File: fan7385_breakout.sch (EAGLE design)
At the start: 13 parts

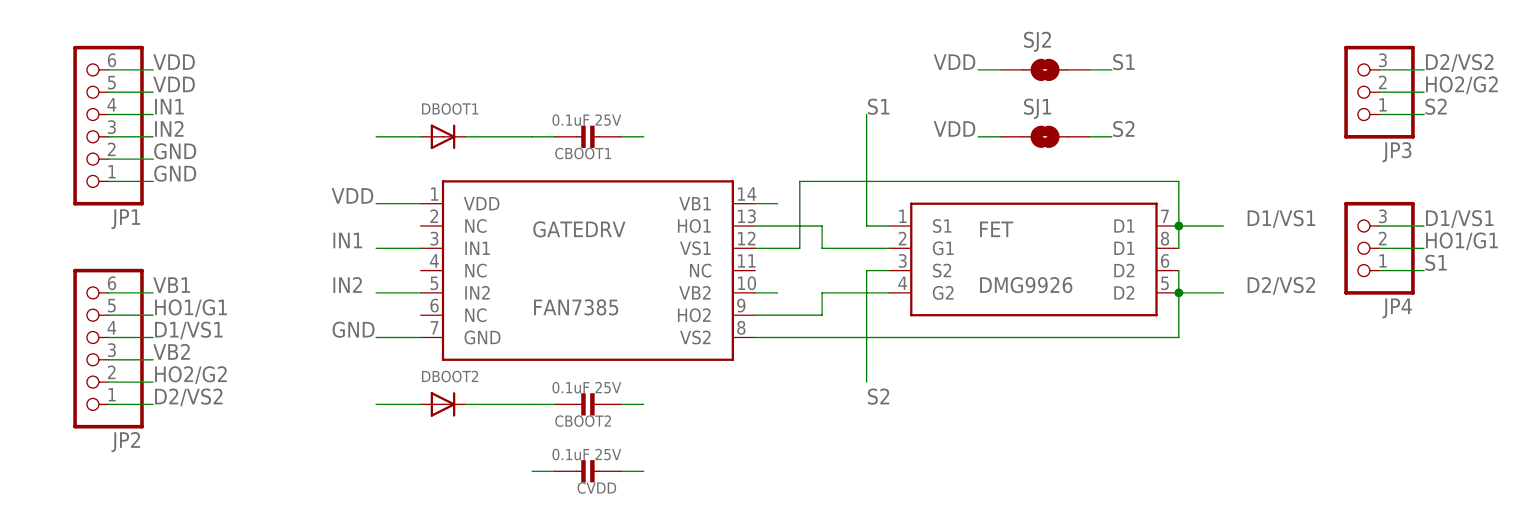
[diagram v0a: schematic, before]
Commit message: make the signal back from drains to the driver normal instead of high-power
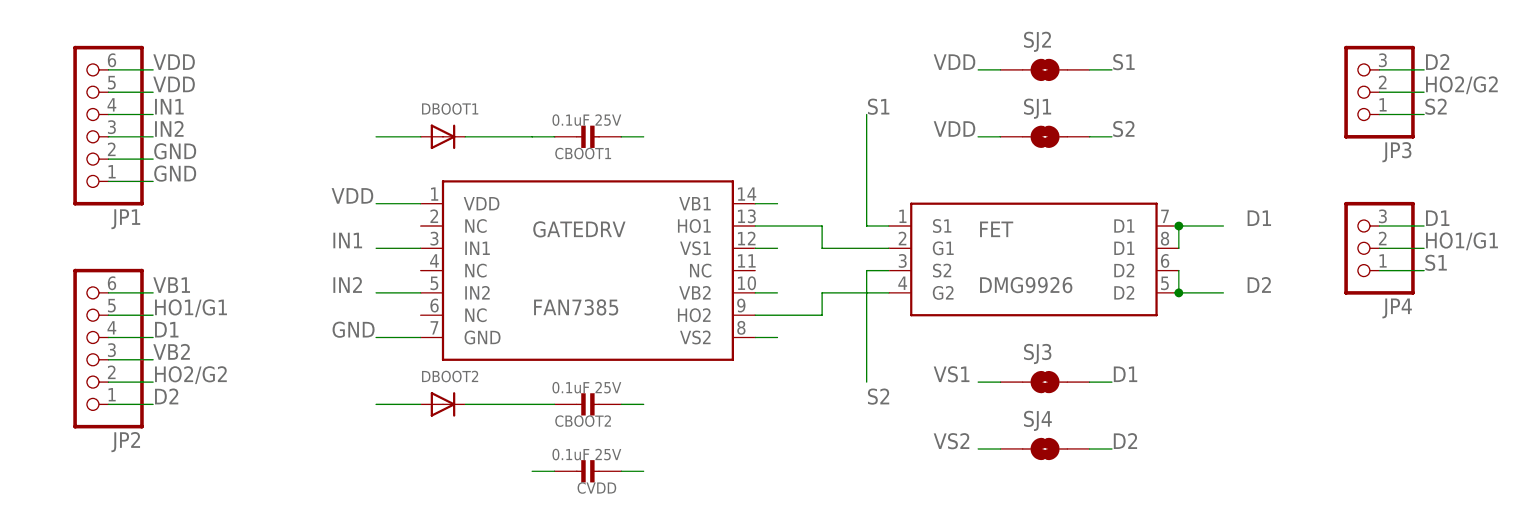
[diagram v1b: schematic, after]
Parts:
- added SJ3, SJ4: SOLDERJUMPERTRACE, SparkFun-Passives:SOLDERJUMPERTRACE
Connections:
- removed net D1/VS1: CBOOT1.P$1, FET.D1@1, FET.D1@2, GATEDRV.VS1, JP2.4, JP4.3
- removed net D2/VS2: CBOOT2.P$1, FET.D2@1, FET.D2@2, GATEDRV.VS2, JP2.1, JP3.3
- new net D1: CBOOT1.P$1, FET.D1@1, FET.D1@2, JP2.4, JP4.3, SJ3.2
- new net D2: CBOOT2.P$1, FET.D2@1, FET.D2@2, JP2.1, JP3.3, SJ4.2
- new net VS1: GATEDRV.VS1, SJ3.1
- new net VS2: GATEDRV.VS2, SJ4.1
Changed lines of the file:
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@@
 <part name="JP3" library="pinhead" deviceset="PINHD-1X3" device=""/>
 <part name="JP4" library="pinhead" deviceset="PINHD-1X3" device=""/>
+<part name="SJ3" library="SparkFun-Passives" deviceset="SOLDERJUMPER" device="TRACE"/>
+<part name="SJ4" library="SparkFun-Passives" deviceset="SOLDERJUMPER" device="TRACE"/>
 </parts>
 <sheets>
@@
 <instance part="JP3" gate="A" x="142.24" y="55.88" rot="R180"/>
 <instance part="JP4" gate="A" x="142.24" y="38.1" rot="R180"/>
+<instance part="SJ3" gate="1" x="106.68" y="22.86" smashed="yes">
+<attribute name="NAME" x="104.14" y="25.4" size="1.778" layer="95"/>
+</instance>
+<instance part="SJ4" gate="1" x="106.68" y="15.24" smashed="yes">
+<attribute name="NAME" x="104.14" y="17.78" size="1.778" layer="95"/>
+</instance>
 </instances>
 <busses>
@@
 </segment>
 </net>
-<net name="D2/VS2" class="2">
+<net name="D2" class="2">
 <segment>
 <pinref part="FET" gate="G$1" pin="D2@1"/>
@@
 <junction x="121.92" y="33.02"/>
 <label x="129.54" y="33.02" size="1.778" layer="95"/>
-<pinref part="GATEDRV" gate="G$1" pin="VS2"/>
-<wire x1="73.66" y1="27.94" x2="121.92" y2="27.94" width="0.1524" layer="91"/>
-<wire x1="121.92" y1="27.94" x2="121.92" y2="33.02" width="0.1524" layer="91"/>
 </segment>
 <segment>
@@
 <label x="149.86" y="58.42" size="1.778" layer="95"/>
 </segment>
-</net>
-<net name="D1/VS1" class="2">
+<segment>
+<pinref part="SJ4" gate="1" pin="2"/>
+<wire x1="111.76" y1="15.24" x2="114.3" y2="15.24" width="0.1524" layer="91"/>
+<label x="114.3" y="15.24" size="1.778" layer="95"/>
+</segment>
+</net>
+<net name="D1" class="2">
 <segment>
 <pinref part="FET" gate="G$1" pin="D1@1"/>
@@
 <junction x="121.92" y="40.64"/>
 <label x="129.54" y="40.64" size="1.778" layer="95"/>
-<wire x1="121.92" y1="40.64" x2="121.92" y2="45.72" width="0.1524" layer="91"/>
-<wire x1="121.92" y1="45.72" x2="78.74" y2="45.72" width="0.1524" layer="91"/>
-<wire x1="78.74" y1="45.72" x2="78.74" y2="38.1" width="0.1524" layer="91"/>
-<pinref part="GATEDRV" gate="G$1" pin="VS1"/>
-<wire x1="78.74" y1="38.1" x2="73.66" y2="38.1" width="0.1524" layer="91"/>
 </segment>
 <segment>
@@
 <label x="149.86" y="40.64" size="1.778" layer="95"/>
 </segment>
-</net>
+<segment>
+<pinref part="SJ3" gate="1" pin="2"/>
+<wire x1="111.76" y1="22.86" x2="114.3" y2="22.86" width="0.1524" layer="91"/>
+<label x="114.3" y="22.86" size="1.778" layer="95"/>
+</segment>
+</net>
+<net name="VS1" class="0">
+<segment>
+<pinref part="GATEDRV" gate="G$1" pin="VS1"/>
+<wire x1="76.2" y1="38.1" x2="73.66" y2="38.1" width="0.1524" layer="91"/>
+</segment>
+<segment>
+<pinref part="SJ3" gate="1" pin="1"/>
+<wire x1="101.6" y1="22.86" x2="99.06" y2="22.86" width="0.1524" layer="91"/>
+<label x="93.98" y="22.86" size="1.778" layer="95"/>
+</segment>
+</net>
+<net name="VS2" class="0">
+<segment>
+<pinref part="GATEDRV" gate="G$1" pin="VS2"/>
+<wire x1="73.66" y1="27.94" x2="76.2" y2="27.94" width="0.1524" layer="91"/>
+</segment>
+<segment>
+<pinref part="SJ4" gate="1" pin="1"/>
+<wire x1="101.6" y1="15.24" x2="99.06" y2="15.24" width="0.1524" layer="91"/>
+<label x="93.98" y="15.24" size="1.778" layer="95"/>
+</segment>
+</net>

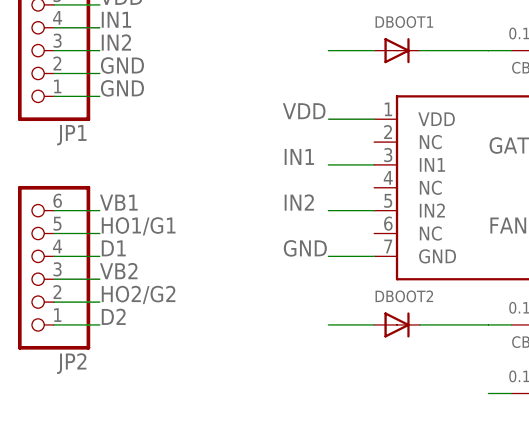
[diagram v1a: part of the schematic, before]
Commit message: one more signal rename
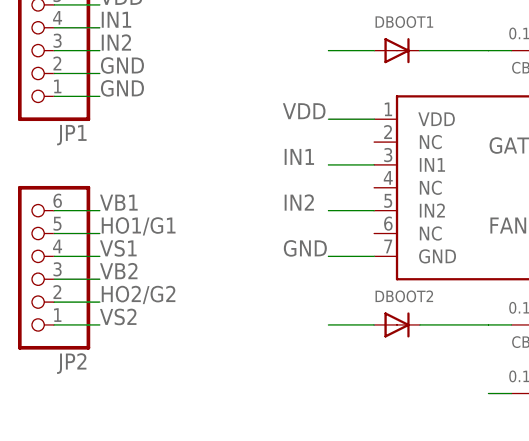
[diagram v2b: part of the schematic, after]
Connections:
- net D1: no longer JP2.4
- net D2: no longer JP2.1
- net VS1: now also JP2.4
- net VS2: now also JP2.1
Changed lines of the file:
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@@
-</segment>
-<segment>
-<pinref part="JP2" gate="A" pin="1"/>
-<wire x1="0" y1="20.32" x2="5.08" y2="20.32" width="0.1524" layer="91"/>
-<label x="5.08" y="20.32" size="1.778" layer="95"/>
 </segment>
 <segment>
@@
 </segment>
 <segment>
-<pinref part="JP2" gate="A" pin="4"/>
-<wire x1="0" y1="27.94" x2="5.08" y2="27.94" width="0.1524" layer="91"/>
-<label x="5.08" y="27.94" size="1.778" layer="95"/>
-</segment>
-<segment>
 <pinref part="JP4" gate="A" pin="3"/>
 <wire x1="144.78" y1="40.64" x2="149.86" y2="40.64" width="0.1524" layer="91"/>
@@
 <label x="93.98" y="22.86" size="1.778" layer="95"/>
 </segment>
+<segment>
+<pinref part="JP2" gate="A" pin="4"/>
+<wire x1="0" y1="27.94" x2="5.08" y2="27.94" width="0.1524" layer="91"/>
+<label x="5.08" y="27.94" size="1.778" layer="95"/>
+</segment>
 </net>
 <net name="VS2" class="0">
@@
 <label x="93.98" y="15.24" size="1.778" layer="95"/>
 </segment>
+<segment>
+<pinref part="JP2" gate="A" pin="1"/>
+<wire x1="0" y1="20.32" x2="5.08" y2="20.32" width="0.1524" layer="91"/>
+<label x="5.08" y="20.32" size="1.778" layer="95"/>
+</segment>
 </net>

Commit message: one more signal rename
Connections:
- net D1: no longer CBOOT1.P$1
- net D2: no longer CBOOT2.P$1
- net VS1: now also CBOOT1.P$1
- net VS2: now also CBOOT2.P$1
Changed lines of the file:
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@@
-</segment>
-<segment>
-<pinref part="CBOOT2" gate="G$1" pin="P$1"/>
-<wire x1="58.42" y1="20.32" x2="60.96" y2="20.32" width="0.1524" layer="91"/>
 </segment>
 <segment>
@@
 <junction x="121.92" y="40.64"/>
 <label x="129.54" y="40.64" size="1.778" layer="95"/>
-</segment>
-<segment>
-<pinref part="CBOOT1" gate="G$1" pin="P$1"/>
-<wire x1="58.42" y1="50.8" x2="60.96" y2="50.8" width="0.1524" layer="91"/>
 </segment>
 <segment>
@@
 <label x="5.08" y="27.94" size="1.778" layer="95"/>
 </segment>
+<segment>
+<pinref part="CBOOT1" gate="G$1" pin="P$1"/>
+<wire x1="58.42" y1="50.8" x2="60.96" y2="50.8" width="0.1524" layer="91"/>
+</segment>
 </net>
 <net name="VS2" class="0">
@@
 <label x="5.08" y="20.32" size="1.778" layer="95"/>
 </segment>
+<segment>
+<pinref part="CBOOT2" gate="G$1" pin="P$1"/>
+<wire x1="58.42" y1="20.32" x2="60.96" y2="20.32" width="0.1524" layer="91"/>
+</segment>
 </net>

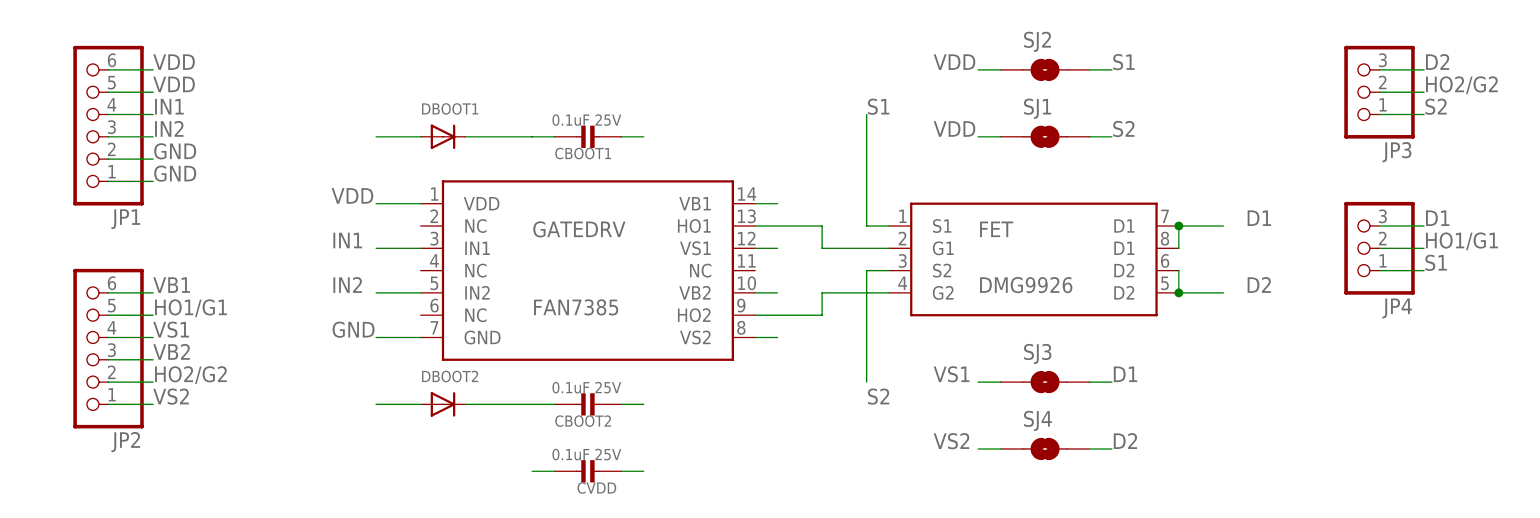
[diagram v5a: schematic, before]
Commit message: diffeent pin header part and 100mil spacing between pins
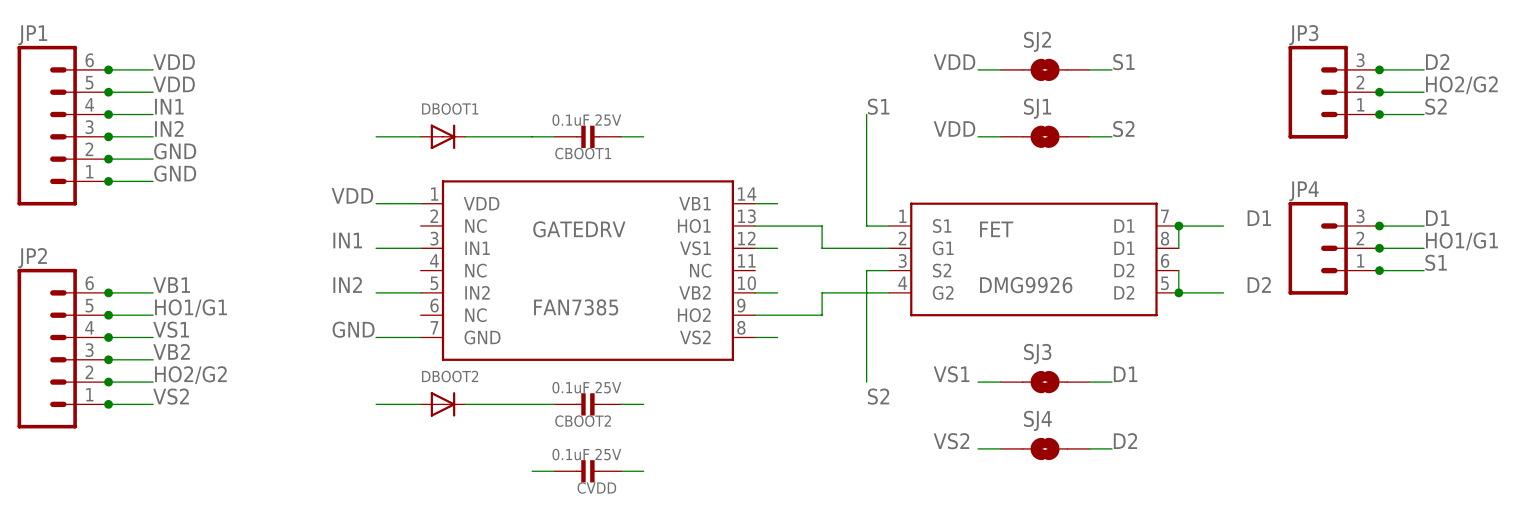
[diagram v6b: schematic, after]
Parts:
- JP1, JP2: device pinhead:PINHD-1X6 -> SparkFun-Connectors:M06SIP
- JP3, JP4: device pinhead:PINHD-1X3 -> SparkFun-Connectors:M03PTH
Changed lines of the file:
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@@
 <layer number="151" name="HeatSink" color="7" fill="1" visible="yes" active="yes"/>
 <layer number="152" name="_bDocu" color="7" fill="1" visible="yes" active="yes"/>
+<layer number="199" name="Contour" color="7" fill="1" visible="yes" active="yes"/>
 <layer number="200" name="200bmp" color="1" fill="10" visible="yes" active="yes"/>
 <layer number="201" name="201bmp" color="7" fill="1" visible="yes" active="yes"/>
@@
 <part name="SJ1" library="SparkFun-Passives" deviceset="SOLDERJUMPER" device="NO"/>
 <part name="SJ2" library="SparkFun-Passives" deviceset="SOLDERJUMPER" device="NO"/>
-<part name="JP1" library="pinhead" deviceset="PINHD-1X6" device=""/>
-<part name="JP2" library="pinhead" deviceset="PINHD-1X6" device=""/>
-<part name="JP3" library="pinhead" deviceset="PINHD-1X3" device=""/>
-<part name="JP4" library="pinhead" deviceset="PINHD-1X3" device=""/>
 <part name="SJ3" library="SparkFun-Passives" deviceset="SOLDERJUMPER" device="TRACE"/>
 <part name="SJ4" library="SparkFun-Passives" deviceset="SOLDERJUMPER" device="TRACE"/>
+<part name="JP1" library="SparkFun-Connectors" deviceset="M06" device="SIP"/>
+<part name="JP2" library="SparkFun-Connectors" deviceset="M06" device="SIP"/>
+<part name="JP3" library="SparkFun-Connectors" deviceset="M03" device="PTH"/>
+<part name="JP4" library="SparkFun-Connectors" deviceset="M03" device="PTH"/>
 </parts>
 <sheets>
@@
 <attribute name="NAME" x="104.14" y="60.96" size="1.778" layer="95"/>
 </instance>
-<instance part="JP1" gate="A" x="-2.54" y="53.34" rot="R180"/>
-<instance part="JP2" gate="A" x="-2.54" y="27.94" rot="R180"/>
-<instance part="JP3" gate="A" x="142.24" y="55.88" rot="R180"/>
-<instance part="JP4" gate="A" x="142.24" y="38.1" rot="R180"/>
 <instance part="SJ3" gate="1" x="106.68" y="22.86" smashed="yes">
 <attribute name="NAME" x="104.14" y="25.4" size="1.778" layer="95"/>
@@
 <attribute name="NAME" x="104.14" y="17.78" size="1.778" layer="95"/>
 </instance>
+<instance part="JP1" gate="G$1" x="-5.08" y="50.8"/>
+<instance part="JP2" gate="G$1" x="-5.08" y="25.4"/>
+<instance part="JP3" gate="G$1" x="137.16" y="55.88"/>
+<instance part="JP4" gate="G$1" x="137.16" y="38.1"/>
 </instances>
 <busses>
@@
 </segment>
 <segment>
-<pinref part="JP1" gate="A" pin="2"/>
 <wire x1="0" y1="48.26" x2="5.08" y2="48.26" width="0.1524" layer="91"/>
 <label x="5.08" y="48.26" size="1.778" layer="95"/>
-</segment>
-<segment>
-<pinref part="JP1" gate="A" pin="1"/>
+<pinref part="JP1" gate="G$1" pin="2"/>
+<junction x="0" y="48.26"/>
+</segment>
+<segment>
 <wire x1="0" y1="45.72" x2="5.08" y2="45.72" width="0.1524" layer="91"/>
 <label x="5.08" y="45.72" size="1.778" layer="95"/>
+<pinref part="JP1" gate="G$1" pin="1"/>
+<junction x="0" y="45.72"/>
 </segment>
 </net>
@@
 </segment>
 <segment>
-<pinref part="JP1" gate="A" pin="6"/>
 <wire x1="0" y1="58.42" x2="5.08" y2="58.42" width="0.1524" layer="91"/>
 <label x="5.08" y="58.42" size="1.778" layer="95"/>
-</segment>
-<segment>
-<pinref part="JP1" gate="A" pin="5"/>
+<pinref part="JP1" gate="G$1" pin="6"/>
+<junction x="0" y="58.42"/>
+</segment>
+<segment>
 <wire x1="0" y1="55.88" x2="5.08" y2="55.88" width="0.1524" layer="91"/>
 <label x="5.08" y="55.88" size="1.778" layer="95"/>
+<pinref part="JP1" gate="G$1" pin="5"/>
+<junction x="0" y="55.88"/>
 </segment>
 </net>
@@
 </segment>
 <segment>
-<pinref part="JP4" gate="A" pin="1"/>
 <wire x1="144.78" y1="35.56" x2="149.86" y2="35.56" width="0.1524" layer="91"/>
 <label x="149.86" y="35.56" size="1.778" layer="95"/>
+<pinref part="JP4" gate="G$1" pin="1"/>
+<junction x="144.78" y="35.56"/>
 </segment>
 </net>
@@
 </segment>
 <segment>
-<pinref part="JP3" gate="A" pin="1"/>
 <wire x1="144.78" y1="53.34" x2="149.86" y2="53.34" width="0.1524" layer="91"/>
 <label x="149.86" y="53.34" size="1.778" layer="95"/>
+<pinref part="JP3" gate="G$1" pin="1"/>
+<junction x="144.78" y="53.34"/>
 </segment>
 </net>
@@
 </segment>
 <segment>
-<pinref part="JP1" gate="A" pin="4"/>
 <wire x1="0" y1="53.34" x2="5.08" y2="53.34" width="0.1524" layer="91"/>
 <label x="5.08" y="53.34" size="1.778" layer="95"/>
+<pinref part="JP1" gate="G$1" pin="4"/>
+<junction x="0" y="53.34"/>
 </segment>
 </net>
@@
 </segment>
 <segment>
-<pinref part="JP1" gate="A" pin="3"/>
 <wire x1="0" y1="50.8" x2="5.08" y2="50.8" width="0.1524" layer="91"/>
 <label x="5.08" y="50.8" size="1.778" layer="95"/>
+<pinref part="JP1" gate="G$1" pin="3"/>
+<junction x="0" y="50.8"/>
 </segment>
 </net>
@@
 </segment>
 <segment>
-<pinref part="JP2" gate="A" pin="5"/>
 <wire x1="0" y1="30.48" x2="5.08" y2="30.48" width="0.1524" layer="91"/>
 <label x="5.08" y="30.48" size="1.778" layer="95"/>
-</segment>
-<segment>
-<pinref part="JP4" gate="A" pin="2"/>
+<pinref part="JP2" gate="G$1" pin="5"/>
+<junction x="0" y="30.48"/>
+</segment>
+<segment>
 <wire x1="144.78" y1="38.1" x2="149.86" y2="38.1" width="0.1524" layer="91"/>
 <label x="149.86" y="38.1" size="1.778" layer="95"/>
+<pinref part="JP4" gate="G$1" pin="2"/>
+<junction x="144.78" y="38.1"/>
 </segment>
 </net>
@@
 </segment>
 <segment>
-<pinref part="JP2" gate="A" pin="2"/>
 <wire x1="0" y1="22.86" x2="5.08" y2="22.86" width="0.1524" layer="91"/>
 <label x="5.08" y="22.86" size="1.778" layer="95"/>
-</segment>
-<segment>
-<pinref part="JP3" gate="A" pin="2"/>
+<pinref part="JP2" gate="G$1" pin="2"/>
+<junction x="0" y="22.86"/>
+</segment>
+<segment>
 <wire x1="144.78" y1="55.88" x2="149.86" y2="55.88" width="0.1524" layer="91"/>
 <label x="149.86" y="55.88" size="1.778" layer="95"/>
+<pinref part="JP3" gate="G$1" pin="2"/>
+<junction x="144.78" y="55.88"/>
 </segment>
 </net>
@@
 </segment>
 <segment>
-<pinref part="JP2" gate="A" pin="6"/>
 <wire x1="0" y1="33.02" x2="5.08" y2="33.02" width="0.1524" layer="91"/>
 <label x="5.08" y="33.02" size="1.778" layer="95"/>
+<pinref part="JP2" gate="G$1" pin="6"/>
+<junction x="0" y="33.02"/>
 </segment>
 </net>
@@
 </segment>
 <segment>
-<pinref part="JP2" gate="A" pin="3"/>
 <wire x1="0" y1="25.4" x2="5.08" y2="25.4" width="0.1524" layer="91"/>
 <label x="5.08" y="25.4" size="1.778" layer="95"/>
+<pinref part="JP2" gate="G$1" pin="3"/>
+<junction x="0" y="25.4"/>
 </segment>
 </net>
@@
 </segment>
 <segment>
-<pinref part="JP3" gate="A" pin="3"/>
 <wire x1="144.78" y1="58.42" x2="149.86" y2="58.42" width="0.1524" layer="91"/>
 <label x="149.86" y="58.42" size="1.778" layer="95"/>
+<pinref part="JP3" gate="G$1" pin="3"/>
+<junction x="144.78" y="58.42"/>
 </segment>
 <segment>
@@
 </segment>
 <segment>
-<pinref part="JP4" gate="A" pin="3"/>
 <wire x1="144.78" y1="40.64" x2="149.86" y2="40.64" width="0.1524" layer="91"/>
 <label x="149.86" y="40.64" size="1.778" layer="95"/>
+<pinref part="JP4" gate="G$1" pin="3"/>
+<junction x="144.78" y="40.64"/>
 </segment>
 <segment>
@@
 </segment>
 <segment>
-<pinref part="JP2" gate="A" pin="4"/>
 <wire x1="0" y1="27.94" x2="5.08" y2="27.94" width="0.1524" layer="91"/>
 <label x="5.08" y="27.94" size="1.778" layer="95"/>
+<pinref part="JP2" gate="G$1" pin="4"/>
+<junction x="0" y="27.94"/>
 </segment>
 <segment>
@@
 </segment>
 <segment>
-<pinref part="JP2" gate="A" pin="1"/>
 <wire x1="0" y1="20.32" x2="5.08" y2="20.32" width="0.1524" layer="91"/>
 <label x="5.08" y="20.32" size="1.778" layer="95"/>
-</segment>
-<segment>
+<pinref part="JP2" gate="G$1" pin="1"/>
+<junction x="0" y="20.32"/>
+</segment>
+<segment>
